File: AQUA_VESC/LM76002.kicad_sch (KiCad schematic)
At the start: 22 parts, among them Q13 2N7002, U10 LM76002, U11 15uH

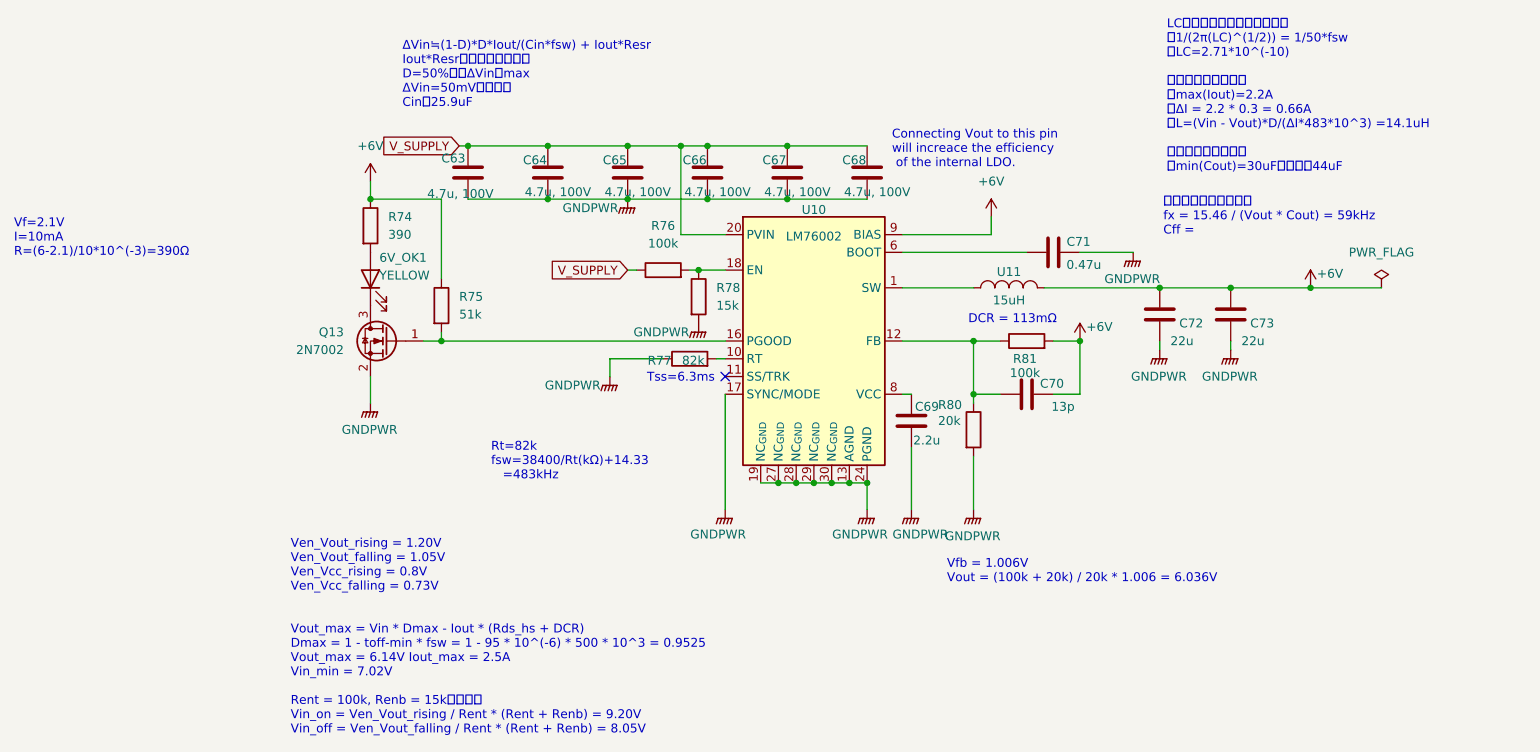
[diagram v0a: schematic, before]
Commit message: 方針変更、back_connector_escにMT60を使用しないことに
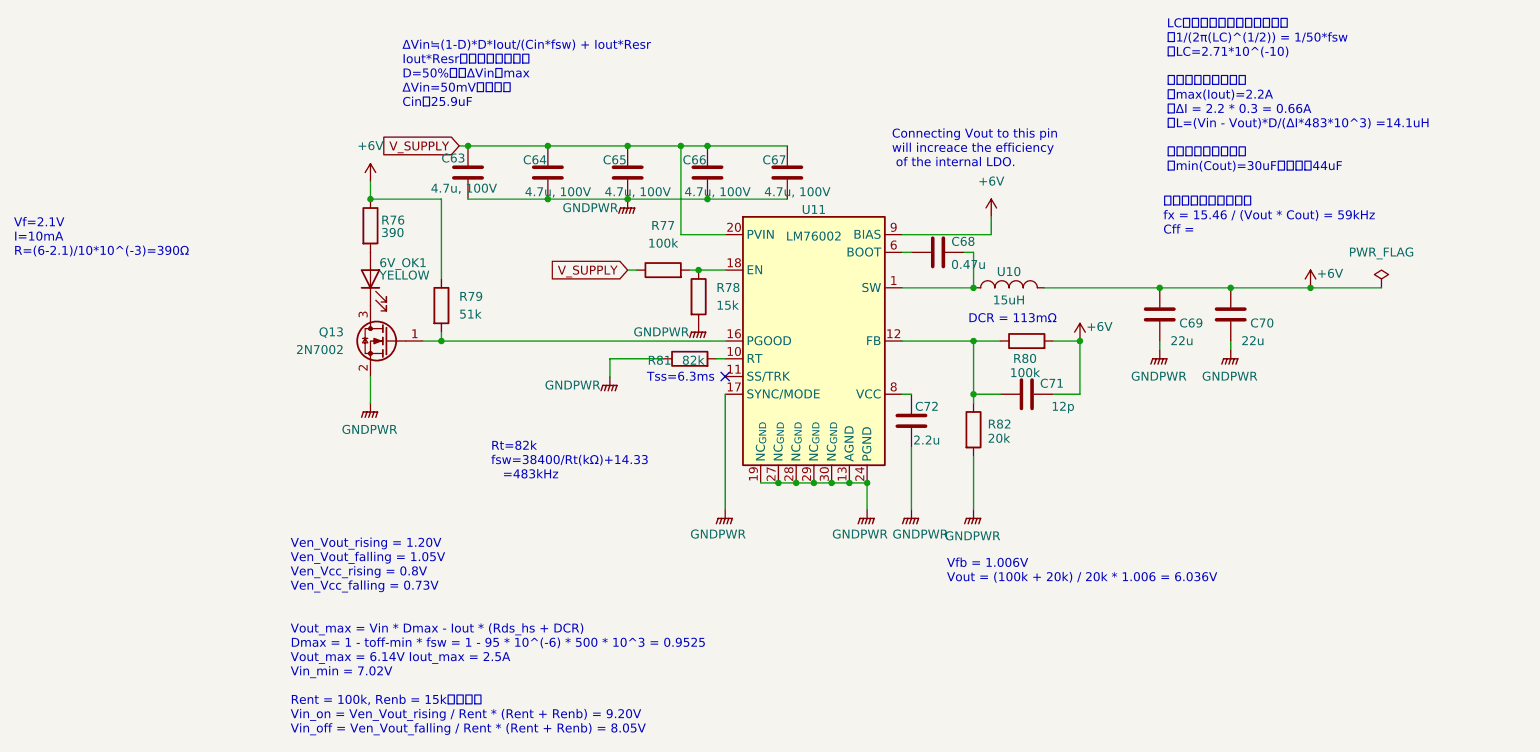
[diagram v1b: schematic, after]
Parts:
- removed C68: 4.7u, 100V, Capacitor_SMD:C_1210_3225Metric, symbol Device:C
- C71: renamed from C70; value 13p -> 12p
- renumbered C71 to C68, C72 to C69, C73 to C70, C69 to C72, R74 to R76, R76 to R77, R75 to R79, R81 to R80, R77 to R81, R80 to R82, U11 to U10, U10 to U11
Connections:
- net GNDPWR: no longer C68.2
- net at U10.1, U11.1 (SW), U11.2 (SW)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: now also C68.2
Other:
- moved on the sheet: C68
